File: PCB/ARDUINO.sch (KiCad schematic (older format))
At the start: 16 parts, among them J1 ICSP, J2 FTDI, SW1 SW_SPST, U1 ATMEGA328P_TQFP, Y1 8MHz

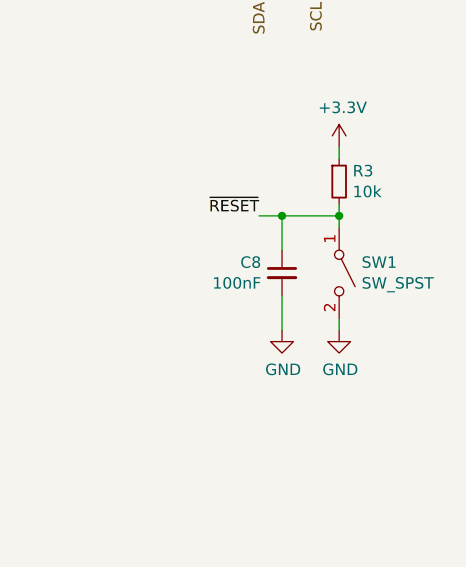
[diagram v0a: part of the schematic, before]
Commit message: Named elements with missing values
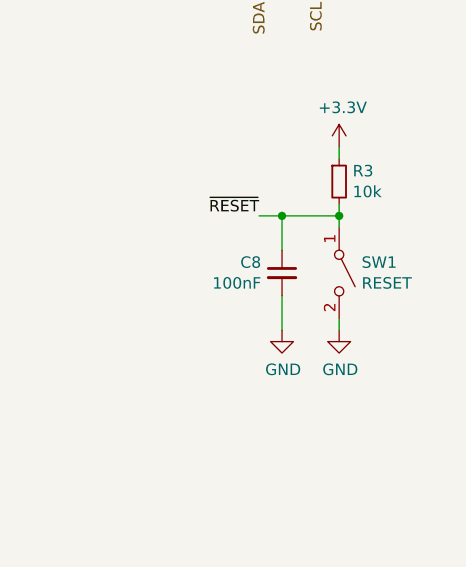
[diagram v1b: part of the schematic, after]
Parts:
- SW1: value SW_SPST -> RESET
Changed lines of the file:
@@
 AR Path="/5E880AC6/5E88BF39" Ref="SW1"  Part="1"
 F 0 "SW1" V 9054 4248 50  0000 L CNN
-F 1 "SW_SPST" V 9145 4248 50  0000 L CNN
+F 1 "RESET" V 9145 4248 50  0000 L CNN
 F 2 "" H 9100 4150 50  0001 C CNN
 F 3 "" H 9100 4150 50  0001 C CNN

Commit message: Added some footprints
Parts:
- U1: footprint TQFP32-08 -> (none)
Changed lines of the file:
@@
 F 0 "U1" H 5150 5300 45  0000 C CNN
 F 1 "ATMEGA328P_TQFP" V 5850 4000 45  0000 C CNN
-F 2 "TQFP32-08" H 5850 5350 20  0001 C CNN
+F 2 "" H 5850 5350 20  0001 C CNN
 F 3 "http://ww1.microchip.com/downloads/en/DeviceDoc/Atmel-7810-Automotive-Microcontrollers-ATmega328P_Datasheet.pdf" H 5850 4000 50  0001 C CNN
 	1    5850 4000

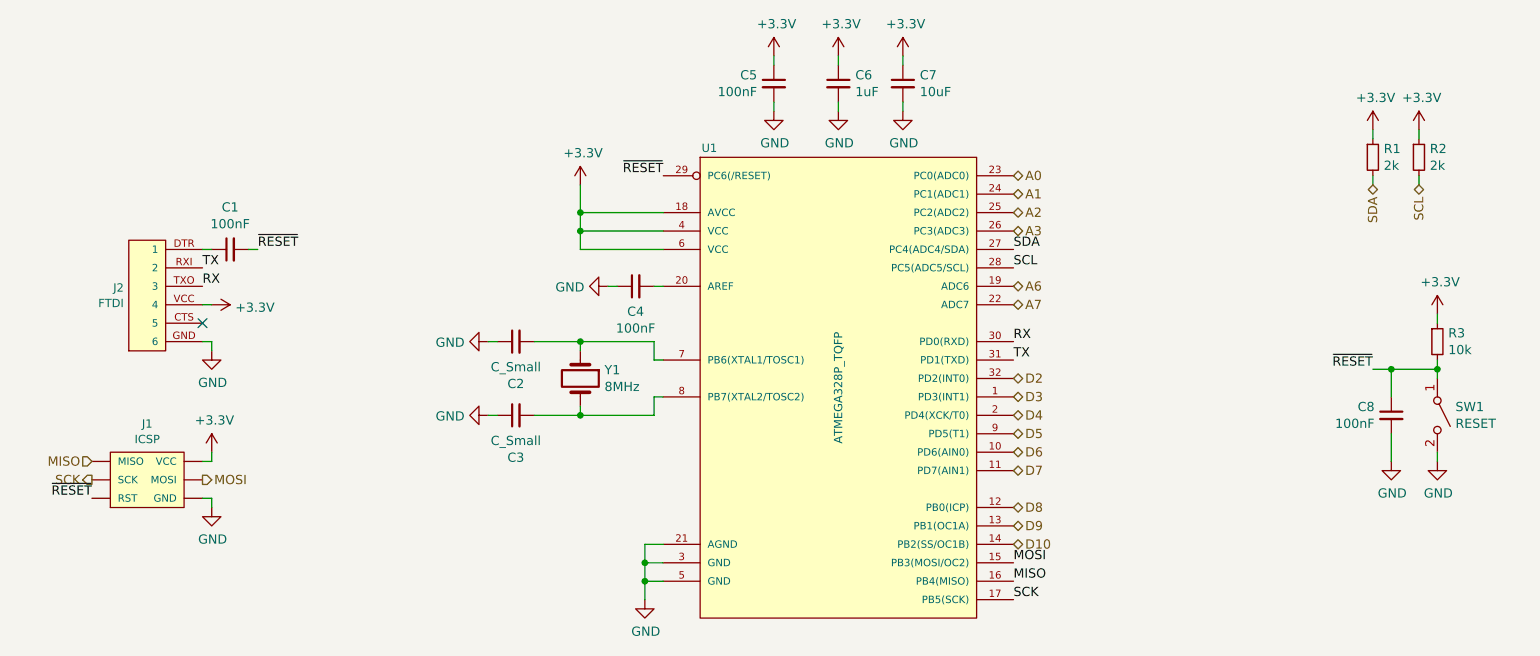
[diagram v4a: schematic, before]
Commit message: Increased VCC from 3v3 to 5v
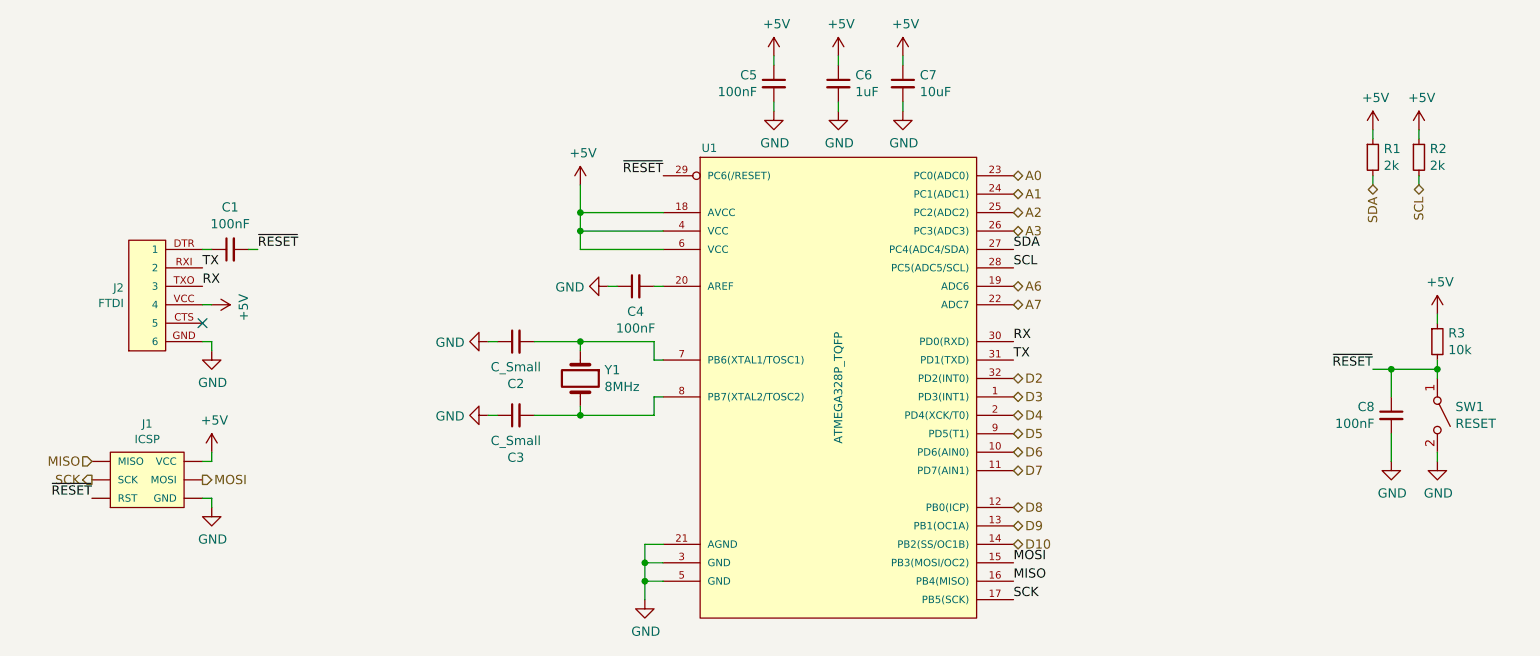
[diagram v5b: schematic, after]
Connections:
- net +3V3 renamed +5V
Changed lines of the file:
@@
 	3950 4150 4000 4150
-$Comp
-L power:+3.3V #PWR?
-U 1 1 5E88BF27
-P 4450 2900
-AR Path="/5E88BF27" Ref="#PWR?"  Part="1"
-AR Path="/5E880AC6/5E88BF27" Ref="#PWR011"  Part="1"
-F 0 "#PWR011" H 4450 2750 50  0001 C CNN
-F 1 "+3.3V" H 4465 3073 50  0000 C CNN
-F 2 "" H 4450 2900 50  0001 C CNN
-F 3 "" H 4450 2900 50  0001 C CNN
-	1    4450 2900
-	1    0    0    -1
-$EndComp
 $Comp
 L power:GND #PWR?
@@
 Wire Wire Line
 	9100 3850 9100 3900
-$Comp
-L power:+3.3V #PWR?
-U 1 1 5E88BF46
-P 9100 3600
-AR Path="/5E88BF46" Ref="#PWR?"  Part="1"
-AR Path="/5E880AC6/5E88BF46" Ref="#PWR023"  Part="1"
-F 0 "#PWR023" H 9100 3450 50  0001 C CNN
-F 1 "+3.3V" H 9115 3773 50  0000 C CNN
-F 2 "" H 9100 3600 50  0001 C CNN
-F 3 "" H 9100 3600 50  0001 C CNN
-	1    9100 3600
-	1    0    0    -1
-$EndComp
 Wire Wire Line
 	9100 3600 9100 3650
@@
 Text Label 1800 4600 2    50   ~ 0
 ~RESET
-$Comp
-L power:+3.3V #PWR?
-U 1 1 5E88BF75
-P 2450 4350
-AR Path="/5E88BF75" Ref="#PWR?"  Part="1"
-AR Path="/5E880AC6/5E88BF75" Ref="#PWR07"  Part="1"
-F 0 "#PWR07" H 2450 4200 50  0001 C CNN
-F 1 "+3.3V" H 2465 4523 50  0000 C CNN
-F 2 "" H 2450 4350 50  0001 C CNN
-F 3 "" H 2450 4350 50  0001 C CNN
-	1    2450 4350
-	1    0    0    -1
-$EndComp
 Wire Wire Line
 	2400 4400 2450 4400
@@
 Wire Wire Line
 	2450 3750 2450 3800
-$Comp
-L power:+3.3V #PWR?
-U 1 1 5E88BFA0
-P 2450 3550
-AR Path="/5E88BFA0" Ref="#PWR?"  Part="1"
-AR Path="/5E880AC6/5E88BFA0" Ref="#PWR05"  Part="1"
-F 0 "#PWR05" H 2450 3400 50  0001 C CNN
-F 1 "+3.3V" V 2465 3678 50  0000 L CNN
-F 2 "" H 2450 3550 50  0001 C CNN
-F 3 "" H 2450 3550 50  0001 C CNN
-	1    2450 3550
-	0    1    1    0
-$EndComp
 Wire Wire Line
 	2450 3550 2400 3550
@@
 Wire Wire Line
 	8750 2900 8750 2850
-$Comp
-L power:+3.3V #PWR?
-U 1 1 5E88BFD5
-P 8750 2600
-AR Path="/5E88BFD5" Ref="#PWR?"  Part="1"
-AR Path="/5E880AC6/5E88BFD5" Ref="#PWR020"  Part="1"
-F 0 "#PWR020" H 8750 2450 50  0001 C CNN
-F 1 "+3.3V" H 8765 2773 50  0000 C CNN
-F 2 "" H 8750 2600 50  0001 C CNN
-F 3 "" H 8750 2600 50  0001 C CNN
-	1    8750 2600
-	1    0    0    -1
-$EndComp
-$Comp
-L power:+3.3V #PWR?
-U 1 1 5E88BFDB
-P 9000 2600
-AR Path="/5E88BFDB" Ref="#PWR?"  Part="1"
-AR Path="/5E880AC6/5E88BFDB" Ref="#PWR022"  Part="1"
-F 0 "#PWR022" H 9000 2450 50  0001 C CNN
-F 1 "+3.3V" H 9015 2773 50  0000 C CNN
-F 2 "" H 9000 2600 50  0001 C CNN
-F 3 "" H 9000 2600 50  0001 C CNN
-	1    9000 2600
-	1    0    0    -1
-$EndComp
 Wire Wire Line
 	9000 2600 9000 2650
@@
 F 3 "" H 6200 2500 50  0001 C CNN
 	1    6200 2500
-	1    0    0    -1
-$EndComp
-$Comp
-L power:+3.3V #PWR?
-U 1 1 5E88C007
-P 5500 2200
-AR Path="/5E88C007" Ref="#PWR?"  Part="1"
-AR Path="/5E880AC6/5E88C007" Ref="#PWR014"  Part="1"
-F 0 "#PWR014" H 5500 2050 50  0001 C CNN
-F 1 "+3.3V" H 5515 2373 50  0000 C CNN
-F 2 "" H 5500 2200 50  0001 C CNN
-F 3 "" H 5500 2200 50  0001 C CNN
-	1    5500 2200
-	1    0    0    -1
-$EndComp
-$Comp
-L power:+3.3V #PWR?
-U 1 1 5E88C00D
-P 5850 2200
-AR Path="/5E88C00D" Ref="#PWR?"  Part="1"
-AR Path="/5E880AC6/5E88C00D" Ref="#PWR016"  Part="1"
-F 0 "#PWR016" H 5850 2050 50  0001 C CNN
-F 1 "+3.3V" H 5865 2373 50  0000 C CNN
-F 2 "" H 5850 2200 50  0001 C CNN
-F 3 "" H 5850 2200 50  0001 C CNN
-	1    5850 2200
-	1    0    0    -1
-$EndComp
-$Comp
-L power:+3.3V #PWR?
-U 1 1 5E88C013
-P 6200 2200
-AR Path="/5E88C013" Ref="#PWR?"  Part="1"
-AR Path="/5E880AC6/5E88C013" Ref="#PWR018"  Part="1"
-F 0 "#PWR018" H 6200 2050 50  0001 C CNN
-F 1 "+3.3V" H 6215 2373 50  0000 C CNN
-F 2 "" H 6200 2200 50  0001 C CNN
-F 3 "" H 6200 2200 50  0001 C CNN
-	1    6200 2200
 	1    0    0    -1
 $EndComp
@@
 Text HLabel 1800 4500 0    50   Output ~ 0
 SCK
+$Comp
+L power:+5V #PWR?
+U 1 1 5E90F2A1
+P 2450 4350
+F 0 "#PWR?" H 2450 4200 50  0001 C CNN
+F 1 "+5V" H 2465 4523 50  0000 C CNN
+F 2 "" H 2450 4350 50  0001 C CNN
+F 3 "" H 2450 4350 50  0001 C CNN
+	1    2450 4350
+	1    0    0    -1
+$EndComp
+$Comp
+L power:+5V #PWR?
+U 1 1 5E910278
+P 2450 3550
+F 0 "#PWR?" H 2450 3400 50  0001 C CNN
+F 1 "+5V" H 2465 3723 50  0000 C CNN
+F 2 "" H 2450 3550 50  0001 C CNN
+F 3 "" H 2450 3550 50  0001 C CNN
+	1    2450 3550
+	0    1    1    0
+$EndComp
+$Comp
+L power:+5V #PWR?
+U 1 1 5E91373A
+P 4450 2900
+AR Path="/5E8A6686/5E91373A" Ref="#PWR?"  Part="1"
+AR Path="/5E880AC6/5E91373A" Ref="#PWR?"  Part="1"
+F 0 "#PWR?" H 4450 2750 50  0001 C CNN
+F 1 "+5V" H 4465 3073 50  0000 C CNN
+F 2 "" H 4450 2900 50  0001 C CNN
+F 3 "" H 4450 2900 50  0001 C CNN
+	1    4450 2900
+	1    0    0    -1
+$EndComp
+$Comp
+L power:+5V #PWR?
+U 1 1 5E914494
+P 5500 2200
+AR Path="/5E8A6686/5E914494" Ref="#PWR?"  Part="1"
+AR Path="/5E880AC6/5E914494" Ref="#PWR?"  Part="1"
+F 0 "#PWR?" H 5500 2050 50  0001 C CNN
+F 1 "+5V" H 5515 2373 50  0000 C CNN
+F 2 "" H 5500 2200 50  0001 C CNN
+F 3 "" H 5500 2200 50  0001 C CNN
+	1    5500 2200
+	1    0    0    -1
+$EndComp
+$Comp
+L power:+5V #PWR?
+U 1 1 5E914816
+P 5850 2200
+AR Path="/5E8A6686/5E914816" Ref="#PWR?"  Part="1"
+AR Path="/5E880AC6/5E914816" Ref="#PWR?"  Part="1"
+F 0 "#PWR?" H 5850 2050 50  0001 C CNN
+F 1 "+5V" H 5865 2373 50  0000 C CNN
+F 2 "" H 5850 2200 50  0001 C CNN
+F 3 "" H 5850 2200 50  0001 C CNN
+	1    5850 2200
+	1    0    0    -1
+$EndComp
+$Comp
+L power:+5V #PWR?
+U 1 1 5E914A94
+P 6200 2200
+AR Path="/5E8A6686/5E914A94" Ref="#PWR?"  Part="1"
+AR Path="/5E880AC6/5E914A94" Ref="#PWR?"  Part="1"
+F 0 "#PWR?" H 6200 2050 50  0001 C CNN
+F 1 "+5V" H 6215 2373 50  0000 C CNN
+F 2 "" H 6200 2200 50  0001 C CNN
+F 3 "" H 6200 2200 50  0001 C CNN
+	1    6200 2200
+	1    0    0    -1
+$EndComp
+$Comp
+L power:+5V #PWR?
+U 1 1 5E9165A4
+P 8750 2600
+F 0 "#PWR?" H 8750 2450 50  0001 C CNN
+F 1 "+5V" H 8765 2773 50  0000 C CNN
+F 2 "" H 8750 2600 50  0001 C CNN
+F 3 "" H 8750 2600 50  0001 C CNN
+	1    8750 2600
+	1    0    0    -1
+$EndComp
+$Comp
+L power:+5V #PWR?
+U 1 1 5E9173BE
+P 9000 2600
+F 0 "#PWR?" H 9000 2450 50  0001 C CNN
+F 1 "+5V" H 9015 2773 50  0000 C CNN
+F 2 "" H 9000 2600 50  0001 C CNN
+F 3 "" H 9000 2600 50  0001 C CNN
+	1    9000 2600
+	1    0    0    -1
+$EndComp
+$Comp
+L power:+5V #PWR?
+U 1 1 5E9181F8
+P 9100 3600
+F 0 "#PWR?" H 9100 3450 50  0001 C CNN
+F 1 "+5V" H 9115 3773 50  0000 C CNN
+F 2 "" H 9100 3600 50  0001 C CNN
+F 3 "" H 9100 3600 50  0001 C CNN
+	1    9100 3600
+	1    0    0    -1
+$EndComp
 $EndSCHEMATC

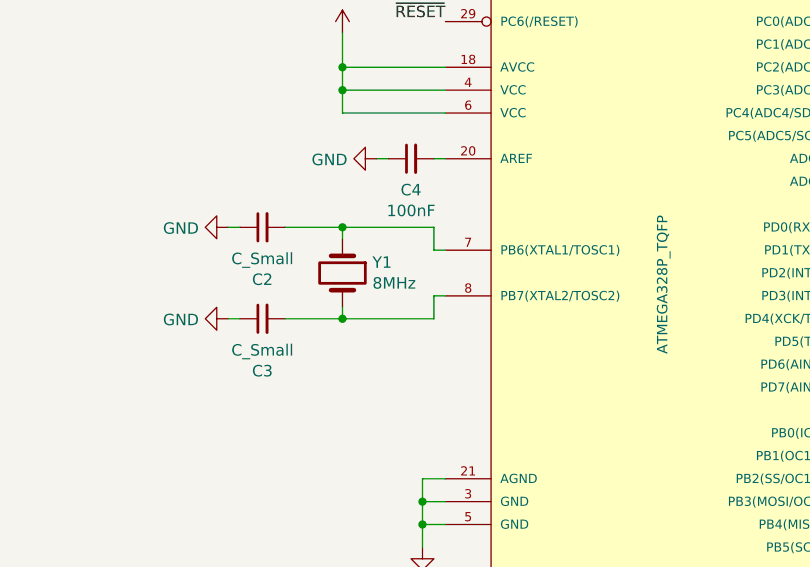
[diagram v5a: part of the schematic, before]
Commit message: Increased MCU XTAL frequency
At 5V it can operate at 16MHz
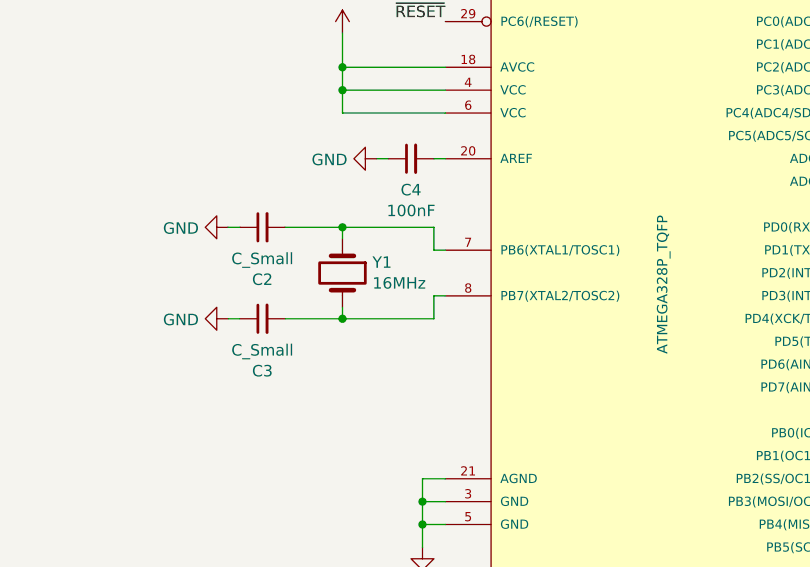
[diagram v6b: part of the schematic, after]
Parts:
- Y1: value 8MHz -> 16MHz
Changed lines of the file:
@@
 AR Path="/5E880AC6/5E88BF03" Ref="Y1"  Part="1"
 F 0 "Y1" V 4404 4081 50  0000 L CNN
-F 1 "8MHz" V 4495 4081 50  0000 L CNN
+F 1 "16MHz" V 4495 4081 50  0000 L CNN
 F 2 "" H 4450 3950 50  0001 C CNN
 F 3 "" H 4450 3950 50  0001 C CNN
@@
 U 1 1 5E90F2A1
 P 2450 4350
+AR Path="/5E8A6686/5E90F2A1" Ref="#PWR?"  Part="1"
+AR Path="/5E880AC6/5E90F2A1" Ref="#PWR?"  Part="1"
 F 0 "#PWR?" H 2450 4200 50  0001 C CNN
 F 1 "+5V" H 2465 4523 50  0000 C CNN
@@
 U 1 1 5E910278
 P 2450 3550
+AR Path="/5E8A6686/5E910278" Ref="#PWR?"  Part="1"
+AR Path="/5E880AC6/5E910278" Ref="#PWR?"  Part="1"
 F 0 "#PWR?" H 2450 3400 50  0001 C CNN
 F 1 "+5V" H 2465 3723 50  0000 C CNN
@@
 U 1 1 5E9165A4
 P 8750 2600
+AR Path="/5E8A6686/5E9165A4" Ref="#PWR?"  Part="1"
+AR Path="/5E880AC6/5E9165A4" Ref="#PWR?"  Part="1"
 F 0 "#PWR?" H 8750 2450 50  0001 C CNN
 F 1 "+5V" H 8765 2773 50  0000 C CNN
@@
 U 1 1 5E9173BE
 P 9000 2600
+AR Path="/5E8A6686/5E9173BE" Ref="#PWR?"  Part="1"
+AR Path="/5E880AC6/5E9173BE" Ref="#PWR?"  Part="1"
 F 0 "#PWR?" H 9000 2450 50  0001 C CNN
 F 1 "+5V" H 9015 2773 50  0000 C CNN
@@
 U 1 1 5E9181F8
 P 9100 3600
+AR Path="/5E8A6686/5E9181F8" Ref="#PWR?"  Part="1"
+AR Path="/5E880AC6/5E9181F8" Ref="#PWR?"  Part="1"
 F 0 "#PWR?" H 9100 3450 50  0001 C CNN
 F 1 "+5V" H 9115 3773 50  0000 C CNN
